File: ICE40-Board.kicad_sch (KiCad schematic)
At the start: 89 parts, among them Q1 2N222, U1 ICE40HX4K-TQ144, U2 ICE40HX4K-TQ144, U3 ICE40HX4K-TQ144, U4 ICE40HX4K-TQ144, U5 ICE40HX4K-TQ144

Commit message: Starting routing
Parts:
- FT_3V3_C1, FT_VCCIN_C1, FT_VCCIO_C1, VBUS_C1: footprint Capacitor_THT:CP_Radial_D12.5mm_P5.00mm -> Capacitor_THT:CP_Radial_D5.0mm_P2.50mm
- IO_H1, IO_H3: symbol Connector_Generic:Conn_02x13_Row_Letter_Last -> Connector_Generic:Conn_02x13_Odd_Even
- IO_H2: symbol Connector_Generic:Conn_02x09_Row_Letter_Last -> Connector_Generic:Conn_02x09_Odd_Even
- JP1: value SolderJumper_2_Bridged -> SCK
- JP2: value SolderJumper_2_Bridged -> MOSI
- JP3: value SolderJumper_2_Bridged -> MISO
- JP4: value SolderJumper_2_Bridged -> SS
- renumbered U5 to U1, U3 to U1, U2 to U1, U4 to U1
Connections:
- net +3V3: now also IO_H1.1 (Pin_1), IO_H2.1 (Pin_1), IO_H3.1 (Pin_1); no longer IO_H1.1a (Pin_1a), IO_H2.1b (Pin_1b), IO_H3.1a (Pin_1a)
- net 10a: now also IO_H1.21 (Pin_21); no longer IO_H1.11a (Pin_11a)
- net 10b: now also IO_H1.22 (Pin_22); no longer IO_H1.11b (Pin_11b)
- net 11a: now also IO_H1.23 (Pin_23); no longer IO_H1.12a (Pin_12a)
- net 11b: now also IO_H1.24 (Pin_24); no longer IO_H1.12b (Pin_12b)
- net 12a: now also IO_H1.25 (Pin_25); no longer IO_H1.13a (Pin_13a)
- net 12b: now also IO_H1.26 (Pin_26); no longer IO_H1.13b (Pin_13b)
- net 13a: now also IO_H2.17 (Pin_17); no longer IO_H2.9b (Pin_9b)
- net 13b: now also IO_H2.18 (Pin_18); no longer IO_H2.9a (Pin_9a)
- net 14a: now also IO_H2.15 (Pin_15); no longer IO_H2.8b (Pin_8b)
- net 14b: now also IO_H2.16 (Pin_16); no longer IO_H2.8a (Pin_8a)
- net 15a: now also IO_H2.13 (Pin_13); no longer IO_H2.7b (Pin_7b)
- net 15b: now also IO_H2.14 (Pin_14); no longer IO_H2.7a (Pin_7a)
- net 16a: now also IO_H2.11 (Pin_11); no longer IO_H2.6b (Pin_6b)
- net 16b: now also IO_H2.12 (Pin_12); no longer IO_H2.6a (Pin_6a)
- net 17a: now also IO_H2.9 (Pin_9); no longer IO_H2.5b (Pin_5b)
- net 17b: now also IO_H2.10 (Pin_10); no longer IO_H2.5a (Pin_5a)
- net 18a: now also IO_H2.7 (Pin_7); no longer IO_H2.4b (Pin_4b)
- net 18b: now also IO_H2.8 (Pin_8); no longer IO_H2.4a (Pin_4a)
- net 19a: now also IO_H2.5 (Pin_5); no longer IO_H2.3b (Pin_3b)
- net 19b: now also IO_H2.6 (Pin_6); no longer IO_H2.3a (Pin_3a)
- net 1a: now also IO_H1.3 (Pin_3); no longer IO_H1.2a (Pin_2a)
- net 1b: now also IO_H1.4 (Pin_4); no longer IO_H1.2b (Pin_2b)
- net 20a: now also IO_H2.3 (Pin_3); no longer IO_H2.2b (Pin_2b)
- net 20b: now also IO_H2.4 (Pin_4); no longer IO_H2.2a (Pin_2a)
- net 21a: now also IO_H3.25 (Pin_25); no longer IO_H3.13a (Pin_13a)
- net 21b: now also IO_H3.26 (Pin_26); no longer IO_H3.13b (Pin_13b)
- net 22a: now also IO_H3.23 (Pin_23); no longer IO_H3.12a (Pin_12a)
- net 22b: now also IO_H3.24 (Pin_24); no longer IO_H3.12b (Pin_12b)
- net 23a: now also IO_H3.21 (Pin_21); no longer IO_H3.11a (Pin_11a)
- net 23b: now also IO_H3.22 (Pin_22); no longer IO_H3.11b (Pin_11b)
- net 24a: now also IO_H3.19 (Pin_19); no longer IO_H3.10a (Pin_10a)
- net 24b: now also IO_H3.20 (Pin_20); no longer IO_H3.10b (Pin_10b)
- net 25a: now also IO_H3.17 (Pin_17); no longer IO_H3.9a (Pin_9a)
- net 25b: now also IO_H3.18 (Pin_18); no longer IO_H3.9b (Pin_9b)
- net 26a: now also IO_H3.15 (Pin_15); no longer IO_H3.8a (Pin_8a)
- net 26b: now also IO_H3.16 (Pin_16); no longer IO_H3.8b (Pin_8b)
- net 27a: now also IO_H3.13 (Pin_13); no longer IO_H3.7a (Pin_7a)
- net 27b: now also IO_H3.14 (Pin_14); no longer IO_H3.7b (Pin_7b)
- net 28a: now also IO_H3.11 (Pin_11); no longer IO_H3.6a (Pin_6a)
- net 28b: now also IO_H3.12 (Pin_12); no longer IO_H3.6b (Pin_6b)
- net 29a: now also IO_H3.9 (Pin_9); no longer IO_H3.5a (Pin_5a)
- net 29b: now also IO_H3.10 (Pin_10); no longer IO_H3.5b (Pin_5b)
- net 2a: now also IO_H1.5 (Pin_5); no longer IO_H1.3a (Pin_3a)
- net 2b: now also IO_H1.6 (Pin_6); no longer IO_H1.3b (Pin_3b)
- net 30a: now also IO_H3.7 (Pin_7); no longer IO_H3.4a (Pin_4a)
- net 30b: now also IO_H3.8 (Pin_8); no longer IO_H3.4b (Pin_4b)
- net 31a: now also IO_H3.5 (Pin_5); no longer IO_H3.3a (Pin_3a)
- net 31b: now also IO_H3.6 (Pin_6); no longer IO_H3.3b (Pin_3b)
- net 32a: now also IO_H3.3 (Pin_3); no longer IO_H3.2a (Pin_2a)
- net 32b: now also IO_H3.4 (Pin_4); no longer IO_H3.2b (Pin_2b)
- net 3a: now also IO_H1.7 (Pin_7); no longer IO_H1.4a (Pin_4a)
- net 3b: now also IO_H1.8 (Pin_8); no longer IO_H1.4b (Pin_4b)
- net 4a: now also IO_H1.9 (Pin_9); no longer IO_H1.5a (Pin_5a)
- net 4b: now also IO_H1.10 (Pin_10); no longer IO_H1.5b (Pin_5b)
- net 5a: now also IO_H1.11 (Pin_11); no longer IO_H1.6a (Pin_6a)
- net 5b: now also IO_H1.12 (Pin_12); no longer IO_H1.6b (Pin_6b)
- net 6a: now also IO_H1.13 (Pin_13); no longer IO_H1.7a (Pin_7a)
- net 6b: now also IO_H1.14 (Pin_14); no longer IO_H1.7b (Pin_7b)
- net 7a: now also IO_H1.15 (Pin_15); no longer IO_H1.8a (Pin_8a)
- net 7b: now also IO_H1.16 (Pin_16); no longer IO_H1.8b (Pin_8b)
- net 8a: now also IO_H1.17 (Pin_17); no longer IO_H1.9a (Pin_9a)
- net 8b: now also IO_H1.18 (Pin_18); no longer IO_H1.9b (Pin_9b)
- net 9a: now also IO_H1.19 (Pin_19); no longer IO_H1.10a (Pin_10a)
- net 9b: now also IO_H1.20 (Pin_20); no longer IO_H1.10b (Pin_10b)
- net GND: now also IO_H1.2 (Pin_2), IO_H2.2 (Pin_2), IO_H3.2 (Pin_2); no longer IO_H1.1b (Pin_1b), IO_H2.1a (Pin_1a), IO_H3.1b (Pin_1b)

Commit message: Changed reference designation method to simple letter + number
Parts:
- renumbered FT_VCCIN_C1 to C1, REG2_C1 to C10, REG2_C2 to C11, REG2_C3 to C12, REG1_C1 to C13, REG1_C2 to C14, REG1_C3 to C15, CLOCK_C1 to C16, VBUS_C1 to C17, VBUS_C2 to C18, CONF_FLASH_C1 to C19, FT_VCCIN_C2 to C2, PROG_FLASH_C1 to C20, FPGA_VCCIO0_C1 to C21, FPGA_VCCIO1_C1 to C22, FPGA_VCCIO2_C1 to C23, FPGA_VCCIO3_C1 to C24, FPGA_2V5_C1 to C25, FPGA_VCC_SPI_C1 to C26, FPGA_C1 to C27, FPGA_C2 to C28, FPGA_C3 to C29, FT_VCCIO_C1 to C3, FPGA_C4 to C30, FPGA_C5 to C31, FPGA_C6 to C32, FPGA_C7 to C33, FPGA_C8 to C34, FPGA_C9 to C35, FPGA_C10 to C36, FT_C3 to C37, FT_C1 to C38, FT_C2 to C39, FT_VCCIO_C2 to C4, FT_3V3_C1 to C5, FT_3V3_C2 to C6, REG3_C1 to C7, REG3_C2 to C8, REG3_C3 to C9, 5V_H1 to H1, FLASH_H11 to H2, SPI_H3 to H3, IO_H1 to IO1, IO_H3 to IO2, IO_H2 to IO3, JP5 to JP1, JP1 to JP2, JP2 to JP3, JP3 to JP4, JP4 to JP5, SCK_R1 to R1, USB_R5 to R10, FT_R5 to R11, PLL_R1 to R12, PLL_R2 to R13, FT_R3 to R14, FT_R4 to R15, FT_R1 to R16, FT_R2 to R17, SS_CONF_R1 to R2, CDONE_R1 to R3, RESET_R1 to R4, USB_R3 to R5, USB_R1 to R6, USB_R4 to R7, USB_R2 to R8, SIT_R1 to R9, REG3 to U1, FTDI1 to U10, REG2 to U2, REG1 to U3, DC_IN1 to U4, CONF_FLASH1 to U5, USB1 to U6, U1 to U7, PROG_FLASH1 to U8, CLOCK1 to U9, VPP_H2 to VPP_H1

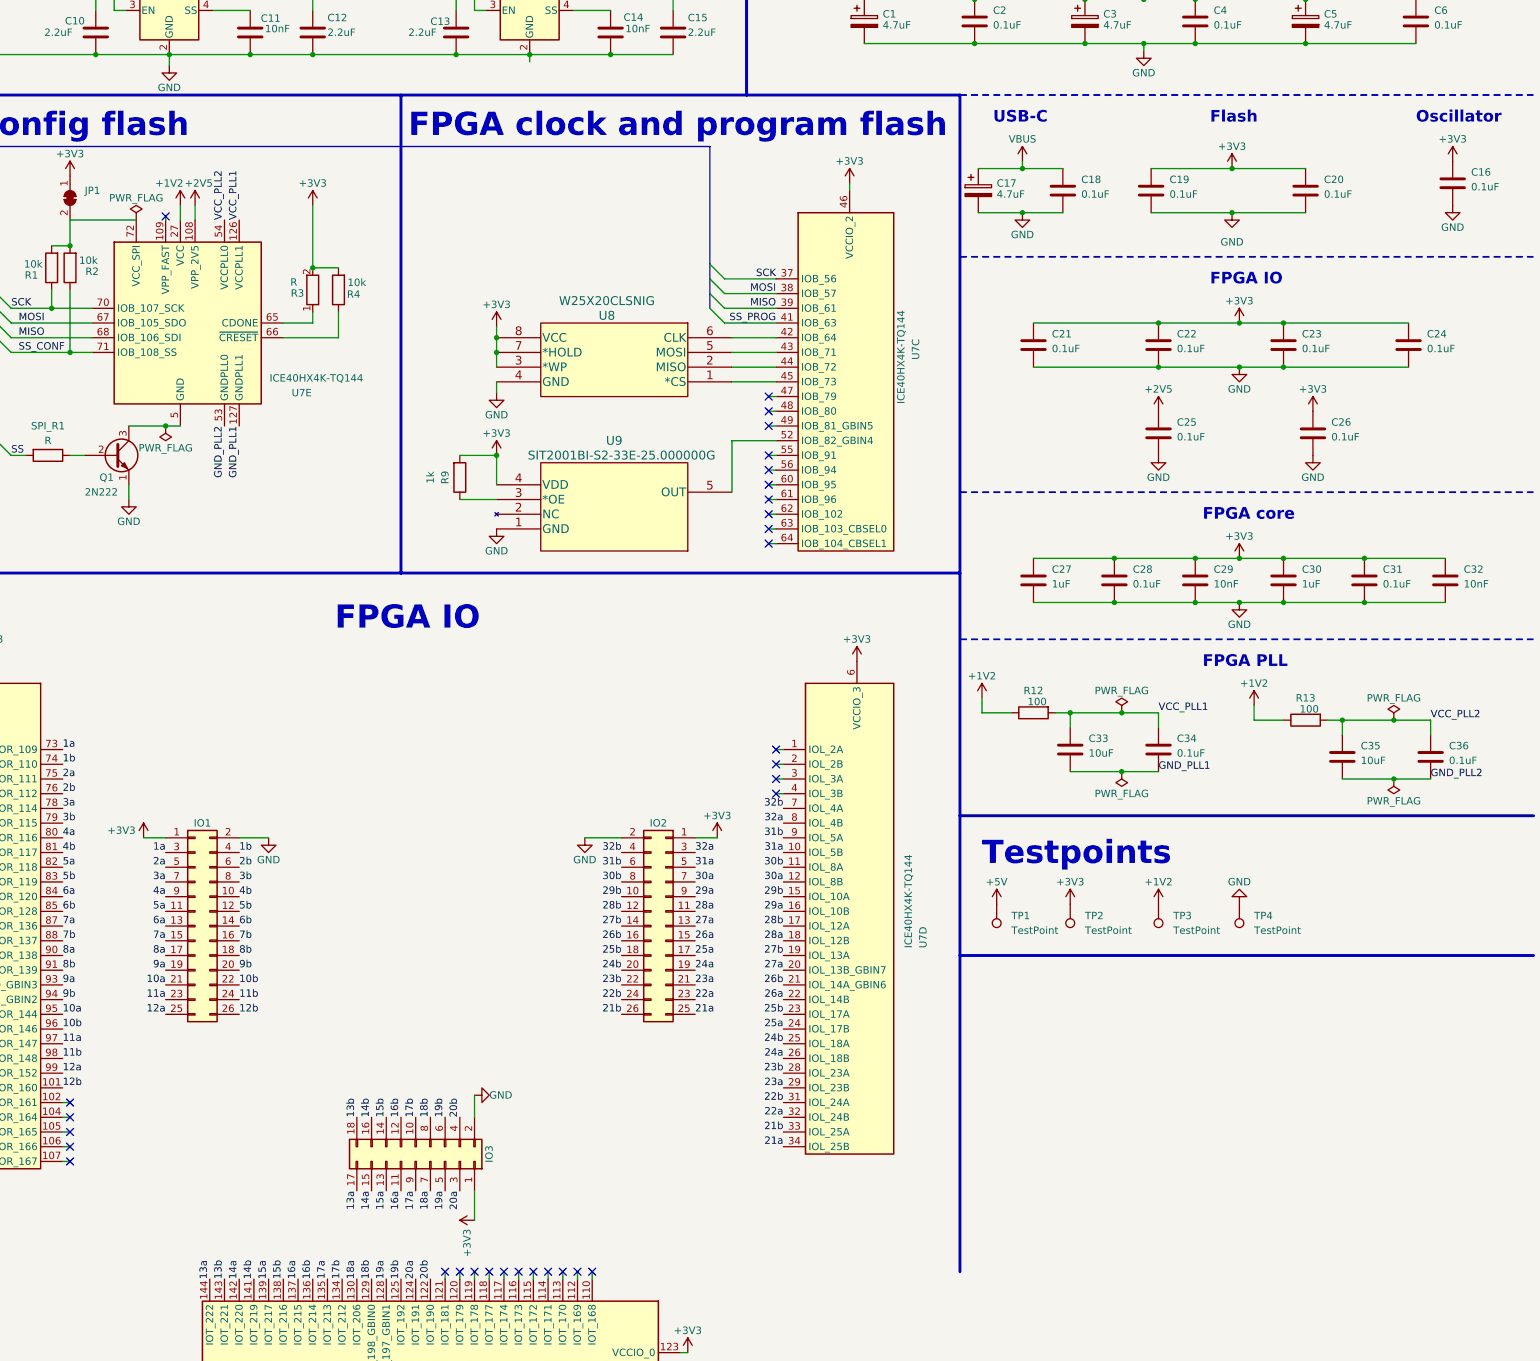
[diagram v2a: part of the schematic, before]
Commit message: Begun initial routing with simple reference designation
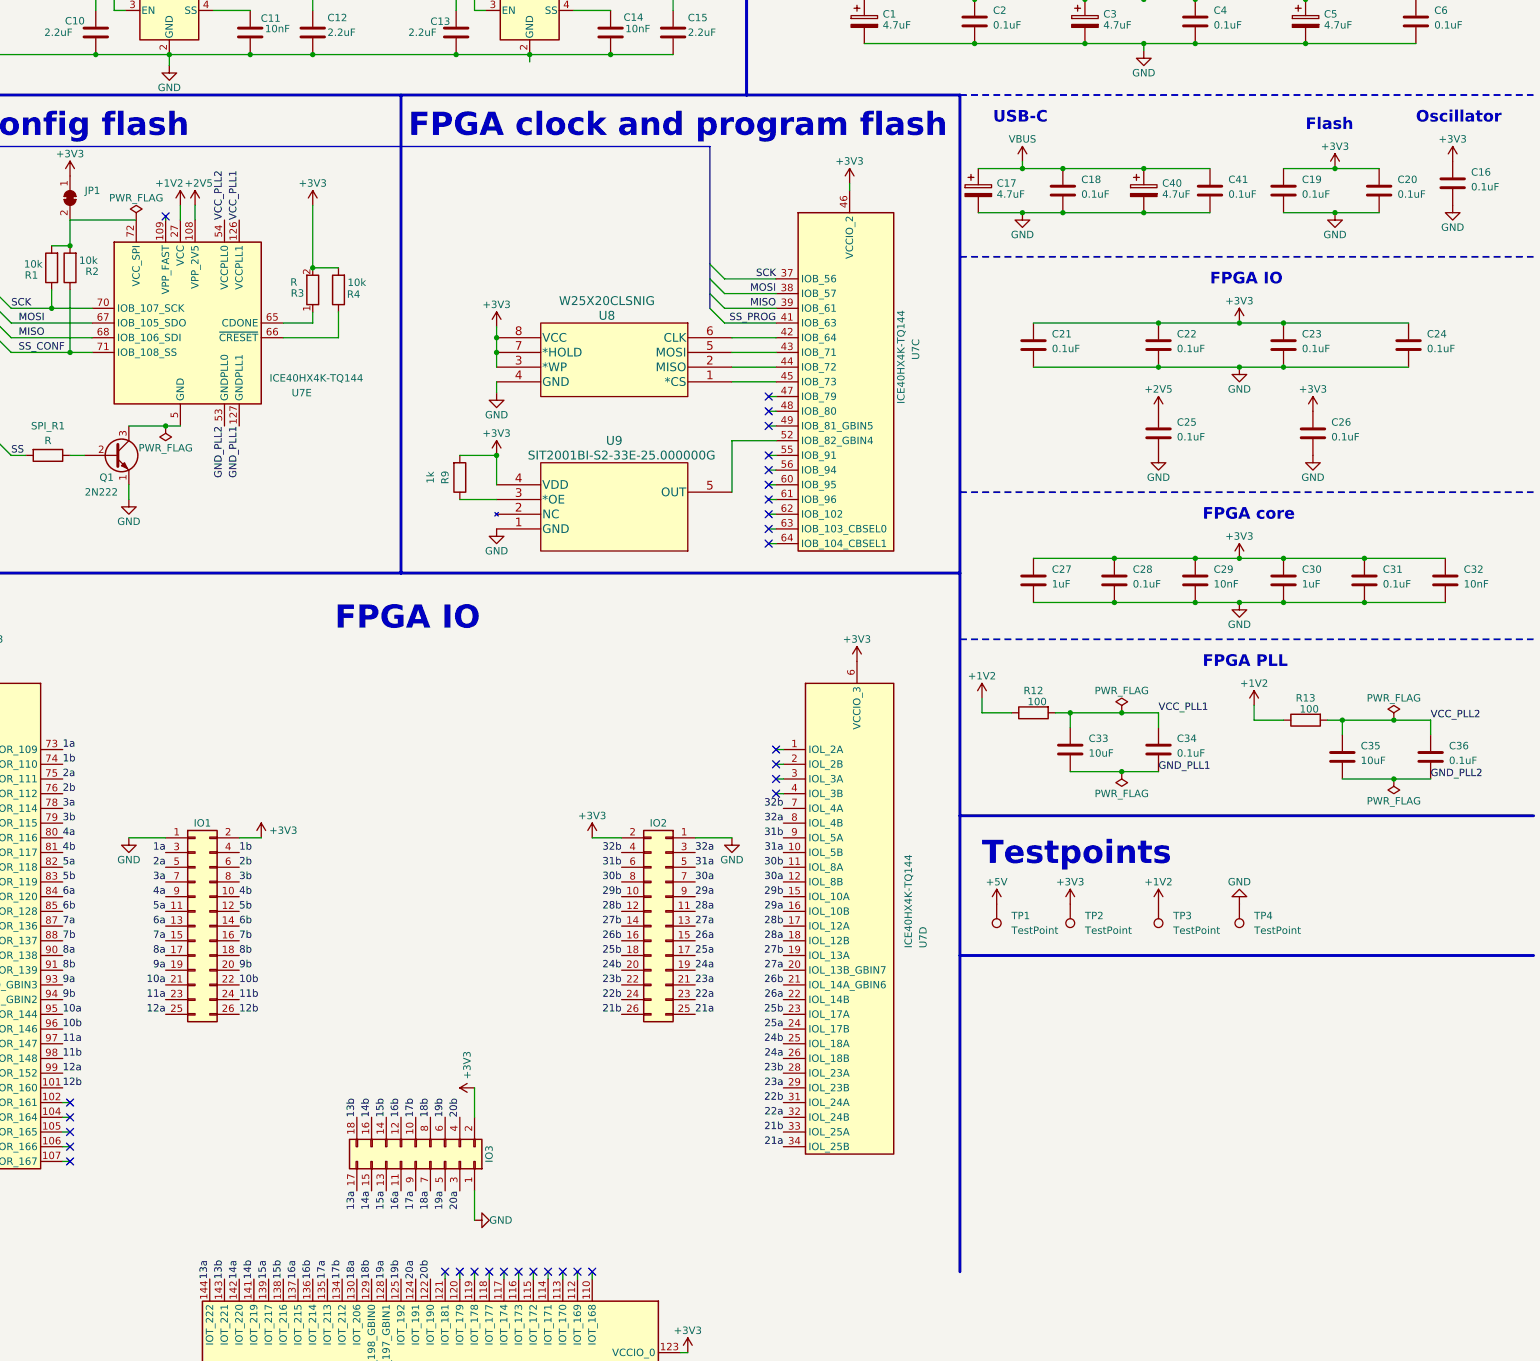
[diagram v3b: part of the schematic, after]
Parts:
- added C40: 4.7uF, Capacitor_THT:CP_Radial_D5.0mm_P2.50mm, symbol Device:C_Polarized
- added C41: 0.1uF, Capacitor_SMD:C_0603_1608Metric, symbol Device:C
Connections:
- net +3V3: now also IO1.2 (Pin_2), IO2.2 (Pin_2), IO3.2 (Pin_2); no longer IO1.1 (Pin_1), IO2.1 (Pin_1), IO3.1 (Pin_1)
- net GND: now also IO1.1 (Pin_1), IO2.1 (Pin_1), IO3.1 (Pin_1), C40.2, C41.2; no longer IO1.2 (Pin_2), IO2.2 (Pin_2), IO3.2 (Pin_2)
- net VBUS: now also C40.1, C41.1
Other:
- moved on the sheet: C19, C20

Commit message: Committing before changing footprints to hand solder version for resistors and capacitors
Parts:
- C1, C17, C3, C40, C5: footprint Capacitor_THT:CP_Radial_D5.0mm_P2.50mm -> Capacitor_THT:CP_Radial_D4.0mm_P2.00mm
- U4: footprint Connector_BarrelJack:BarrelJack_Horizontal -> CUI_PJ-007:CUI_PJ-007
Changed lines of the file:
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@@
     (property "Reference" "U4" (id 0) (at 29.21 30.48 0))
     (property "Value" "Barrel_Jack" (id 1) (at 29.21 32.385 0))
-    (property "Footprint" "Connector_BarrelJack:BarrelJack_Horizontal" (id 2) (at 30.48 39.116 0)
+    (property "Footprint" "CUI_PJ-007:CUI_PJ-007" (id 2) (at 30.48 39.116 0)
       (effects (font (size 1.27 1.27)) hide)
     )
@@
       (effects (font (size 1.27 1.27)) (justify left))
     )
-    (property "Footprint" "Capacitor_THT:CP_Radial_D5.0mm_P2.50mm" (id 2) (at 293.0652 40.64 0)
+    (property "Footprint" "Capacitor_THT:CP_Radial_D4.0mm_P2.00mm" (id 2) (at 293.0652 40.64 0)
       (effects (font (size 1.27 1.27)) hide)
     )
@@
       (effects (font (size 1.27 1.27)) (justify left))
     )
-    (property "Footprint" "Capacitor_THT:CP_Radial_D5.0mm_P2.50mm" (id 2) (at 312.7502 69.85 0)
+    (property "Footprint" "Capacitor_THT:CP_Radial_D4.0mm_P2.00mm" (id 2) (at 312.7502 69.85 0)
       (effects (font (size 1.27 1.27)) hide)
     )
@@
       (effects (font (size 1.27 1.27)) (justify left))
     )
-    (property "Footprint" "Capacitor_THT:CP_Radial_D5.0mm_P2.50mm" (id 2) (at 369.2652 40.64 0)
+    (property "Footprint" "Capacitor_THT:CP_Radial_D4.0mm_P2.00mm" (id 2) (at 369.2652 40.64 0)
       (effects (font (size 1.27 1.27)) hide)
     )
@@
       (effects (font (size 1.27 1.27)) (justify left))
     )
-    (property "Footprint" "Capacitor_THT:CP_Radial_D5.0mm_P2.50mm" (id 2) (at 341.3252 69.85 0)
+    (property "Footprint" "Capacitor_THT:CP_Radial_D4.0mm_P2.00mm" (id 2) (at 341.3252 69.85 0)
       (effects (font (size 1.27 1.27)) hide)
     )
@@
       (effects (font (size 1.27 1.27)) (justify left))
     )
-    (property "Footprint" "Capacitor_THT:CP_Radial_D5.0mm_P2.50mm" (id 2) (at 331.1652 40.64 0)
+    (property "Footprint" "Capacitor_THT:CP_Radial_D4.0mm_P2.00mm" (id 2) (at 331.1652 40.64 0)
       (effects (font (size 1.27 1.27)) hide)
     )
@@
     )
     (path "/3e44de97-8dad-450f-9a3b-be7c19f02009"
-      (reference "C1") (unit 1) (value "4.7uF") (footprint "Capacitor_THT:CP_Radial_D5.0mm_P2.50mm")
+      (reference "C1") (unit 1) (value "4.7uF") (footprint "Capacitor_THT:CP_Radial_D4.0mm_P2.00mm")
     )
     (path "/632e1a1c-c069-4715-ac2e-23038c43539c"
@@
     )
     (path "/a23ecd90-bb9b-4fd2-a42b-7100bfc791b5"
-      (reference "C3") (unit 1) (value "4.7uF") (footprint "Capacitor_THT:CP_Radial_D5.0mm_P2.50mm")
+      (reference "C3") (unit 1) (value "4.7uF") (footprint "Capacitor_THT:CP_Radial_D4.0mm_P2.00mm")
     )
     (path "/765042ad-8833-41d5-b953-c476cc4bd479"
@@
     )
     (path "/94765dbf-ec5f-4465-9753-2016eccc63b1"
-      (reference "C5") (unit 1) (value "4.7uF") (footprint "Capacitor_THT:CP_Radial_D5.0mm_P2.50mm")
+      (reference "C5") (unit 1) (value "4.7uF") (footprint "Capacitor_THT:CP_Radial_D4.0mm_P2.00mm")
     )
     (path "/8b5502ad-202f-4eae-95db-52d7aca717d1"
@@
     )
     (path "/86a66eb8-dea9-4995-92f8-e6370f3aac03"
-      (reference "C17") (unit 1) (value "4.7uF") (footprint "Capacitor_THT:CP_Radial_D5.0mm_P2.50mm")
+      (reference "C17") (unit 1) (value "4.7uF") (footprint "Capacitor_THT:CP_Radial_D4.0mm_P2.00mm")
     )
     (path "/a3732dc0-083c-449e-a00e-18270d4346f1"
@@
     )
     (path "/989450e4-1c8d-4d15-ae3a-54a5520bb694"
-      (reference "C40") (unit 1) (value "4.7uF") (footprint "Capacitor_THT:CP_Radial_D5.0mm_P2.50mm")
+      (reference "C40") (unit 1) (value "4.7uF") (footprint "Capacitor_THT:CP_Radial_D4.0mm_P2.00mm")
     )
     (path "/b833d3b5-3f9d-4954-a2eb-59a1dd4179f7"
@@
     )
     (path "/1c76aae3-bd94-4b78-a171-6b6542da96a4"
-      (reference "U4") (unit 1) (value "Barrel_Jack") (footprint "Connector_BarrelJack:BarrelJack_Horizontal")
+      (reference "U4") (unit 1) (value "Barrel_Jack") (footprint "CUI_PJ-007:CUI_PJ-007")
     )
     (path "/7a6b9cdf-f13b-4329-9d9a-e43f6041b320"

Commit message: Initial routing
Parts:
- removed C1, C17, C3, C40, C5: 4.7uF, Capacitor_THT:CP_Radial_D4.0mm_P2.00mm, symbol Device:C_Polarized
- removed C41: 0.1uF, Capacitor_SMD:C_0603_1608Metric, symbol Device:C
- removed JP1: SolderJumper_2_Bridged, Jumper:SolderJumper-2_P1.3mm_Bridged_Pad1.0x1.5mm, symbol Jumper:SolderJumper_2_Bridged
- removed R13: 100, Resistor_SMD:R_0603_1608Metric, symbol Device:R
- removed TP1, TP2, TP3, TP4: TestPoint, TestPoint:TestPoint_Pad_D1.5mm, symbol Connector:TestPoint
- C10, C11, C12, C13, C14, C15, C16, C18, C19, C2, C20, C21, C22, C23, C24, C25, C26, C28, C31, C33, C34, C36, C37, C38, C39, C4, C6, C7, C8, C9: footprint Capacitor_SMD:C_0603_1608Metric -> Capacitor_SMD:C_0603_1608Metric_Pad1.08x0.95mm_HandSolder
- C27, C30: value 1uF -> 0.1uF; footprint Capacitor_SMD:C_0603_1608Metric -> Capacitor_SMD:C_0603_1608Metric_Pad1.08x0.95mm_HandSolder
- C29, C32: value 10nF -> 0.1uF; footprint Capacitor_SMD:C_0603_1608Metric -> Capacitor_SMD:C_0603_1608Metric_Pad1.08x0.95mm_HandSolder
- C35: value 10uF -> 0.1uF; footprint Capacitor_SMD:C_0603_1608Metric -> Capacitor_SMD:C_0603_1608Metric_Pad1.08x0.95mm_HandSolder
- R1, R10, R11, R12, R14, R15, R16, R17, R2, R3, R4, R5, R6, R7, R8, R9, SPI_R1: footprint Resistor_SMD:R_0603_1608Metric -> Resistor_SMD:R_0603_1608Metric_Pad0.98x0.95mm_HandSolder
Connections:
- net +1V2: now also C27.1, C28.1, C29.1, C30.1
- net +3V3: now also C35.1, C36.1, Q1.3 (C); no longer C27.1, C28.1, C29.1, C30.1
- net GND: now also C35.2, C36.2, U7.103 (GND), U7.13 (GND), U7.132 (GND), U7.14 (GND), U7.140 (GND), U7.5 (GND), U7.59 (GND), U7.69 (GND), U7.86 (GND); no longer Q1.1 (E)
- net GND_PLL1: now also U7.53 (GNDPLL0)
- net MISO: now also H3.4 (Pin_4); no longer H3.3 (Pin_3)
- net MOSI: now also H3.3 (Pin_3); no longer H3.4 (Pin_4)
- net VCC_PLL1: now also U7.54 (VCCPLL0)
- net at R1.2, R2.2, U7.72 (VCC_SPI): now also Q1.1 (E)
- removed net GND_PLL2: C35.2, C36.2, U7.53 (GNDPLL0)
- removed net VCC_PLL2: C35.1, C36.1, U7.54 (VCCPLL0)
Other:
- note added: "2V5 bypass"
- note added: "Each VCCIO_X has two power inputs, have one bypass for each of them"
- note added: "FPGA"
- note added: "One bypass for each VCC pin"
- note added: "PLL Filter"
- note added: "VCC_SPI bypass"
- note removed: "FPGA PLL"
- note removed: "FPGA core"
- note removed: "Testpoints"
- moved on the sheet: C18, C21, C22, C23, C24, C25, C26, C27, C28, C29, C30, H2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
